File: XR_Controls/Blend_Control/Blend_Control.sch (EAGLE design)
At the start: 4 parts

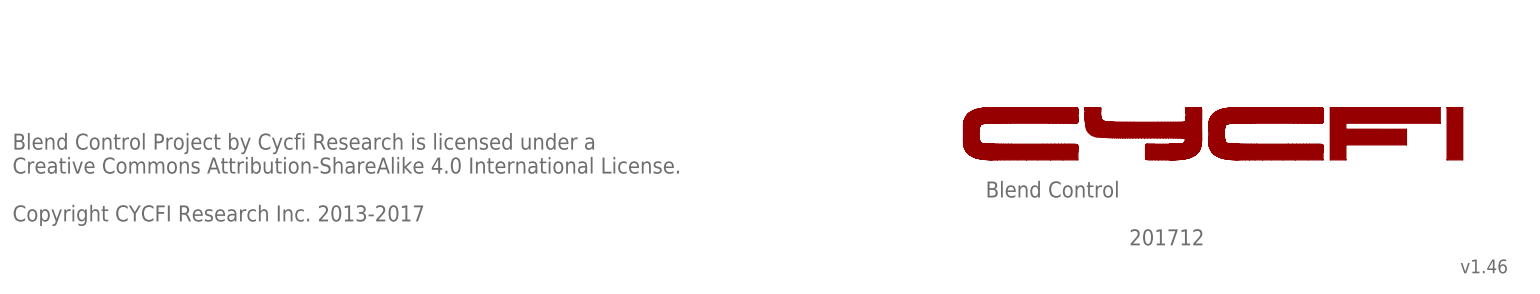
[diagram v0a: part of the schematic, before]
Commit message: Updated broken .sch files
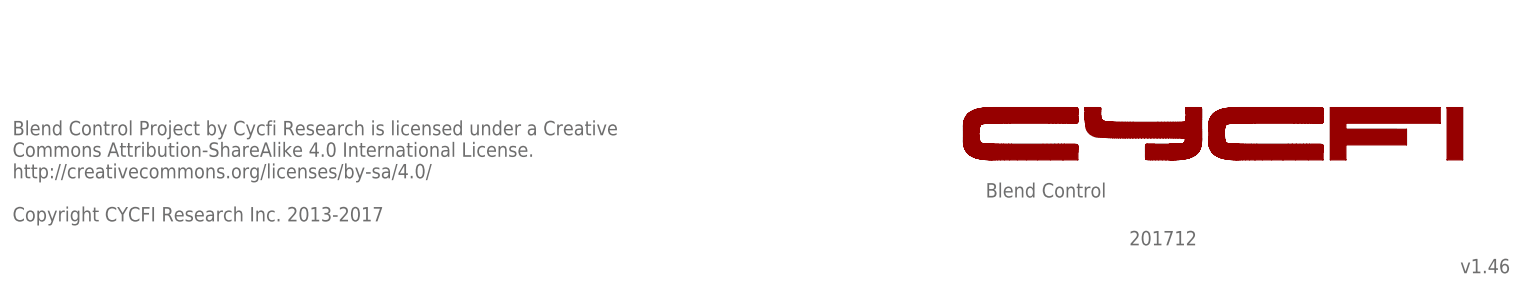
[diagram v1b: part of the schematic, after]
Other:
- note added: "Blend Control Project by Cycfi Research is licensed under a Creative Commons Attribution-ShareAlike 4.0 International License. http://creativecommons.org/licenses/by-sa/4.0/ Copyright CYCFI Research Inc. 2013-2017"
- note removed: "Blend Control Project by Cycfi Research is licensed under a Creative Commons Attribution-ShareAlike 4.0 International License. Copyright CYCFI Research Inc. 2013-2017"
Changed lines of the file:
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@@
 <text x="100.33" y="102.87" size="1.778" layer="95">POT1
 25K</text>
-<text x="177.8" y="19.05" size="2.54" layer="95">Blend Control</text>
-<text x="253.365" y="6.985" size="2.1844" layer="95">v1.46</text>
-<text x="22.86" y="15.24" size="2.54" layer="95">Blend Control Project by Cycfi Research is licensed under a
-Creative Commons Attribution-ShareAlike 4.0 International License.
+<text x="177.8" y="19.05" size="2.286" layer="95" font="vector">Blend Control</text>
+<text x="253.365" y="6.985" size="2.286" layer="95" font="vector">v1.46</text>
+<text x="22.86" y="15.24" size="2.286" layer="95" font="vector">Blend Control Project by Cycfi Research is licensed under a Creative
+Commons Attribution-ShareAlike 4.0 International License.
+http://creativecommons.org/licenses/by-sa/4.0/
 Copyright CYCFI Research Inc. 2013-2017</text>
-<text x="200.66" y="11.43" size="2.54" layer="95">201712</text>
+<text x="200.66" y="11.43" size="2.286" layer="95" font="vector">201712</text>
 <wire x1="192.47528125" y1="25.047221875" x2="190.115640625" y2="25.047221875" width="0" layer="94"/>
 <wire x1="190.115640625" y1="25.047221875" x2="188.10833125" y2="25.047225" width="0" layer="94"/>
@@
 <instance part="FRAME1" gate="G$2" x="162.56" y="0" smashed="yes">
 <attribute name="LAST_DATE_TIME" x="175.26" y="1.27" size="2.54" layer="94" font="vector"/>
-<attribute name="SHEET" x="248.92" y="1.27" size="2.54" layer="94" font="vector"/>
+<attribute name="SHEET" x="248.92" y="1.27" size="2.286" layer="94" font="vector"/>
 </instance>
 </instances>
